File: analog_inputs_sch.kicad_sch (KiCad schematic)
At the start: 52 parts, among them J1 Conn_Coaxial, J2 Conn_Coaxial, K1 Relay_SPDT, K2 Relay_SPDT, K3 Relay_SPDT, K4 Relay_SPDT, K5 Relay_SPDT, K6 Relay_SPDT, U1 OPA656U, U15 OPA2277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

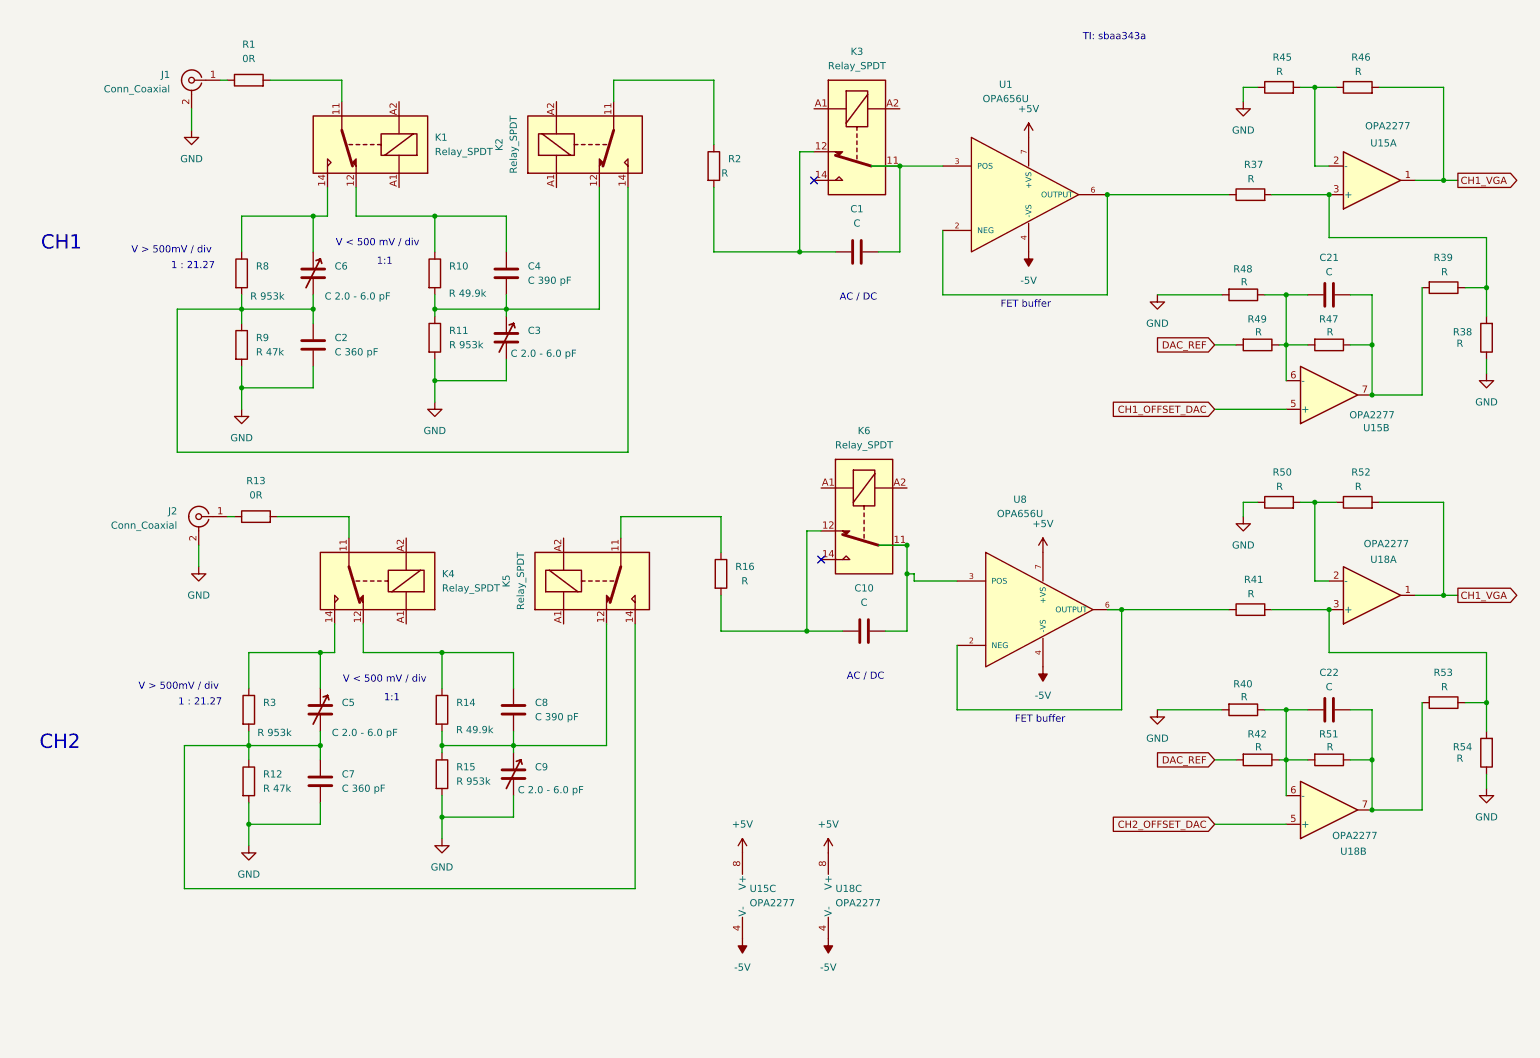
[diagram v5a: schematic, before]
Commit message: PCB edge, initial work on assigning footprints
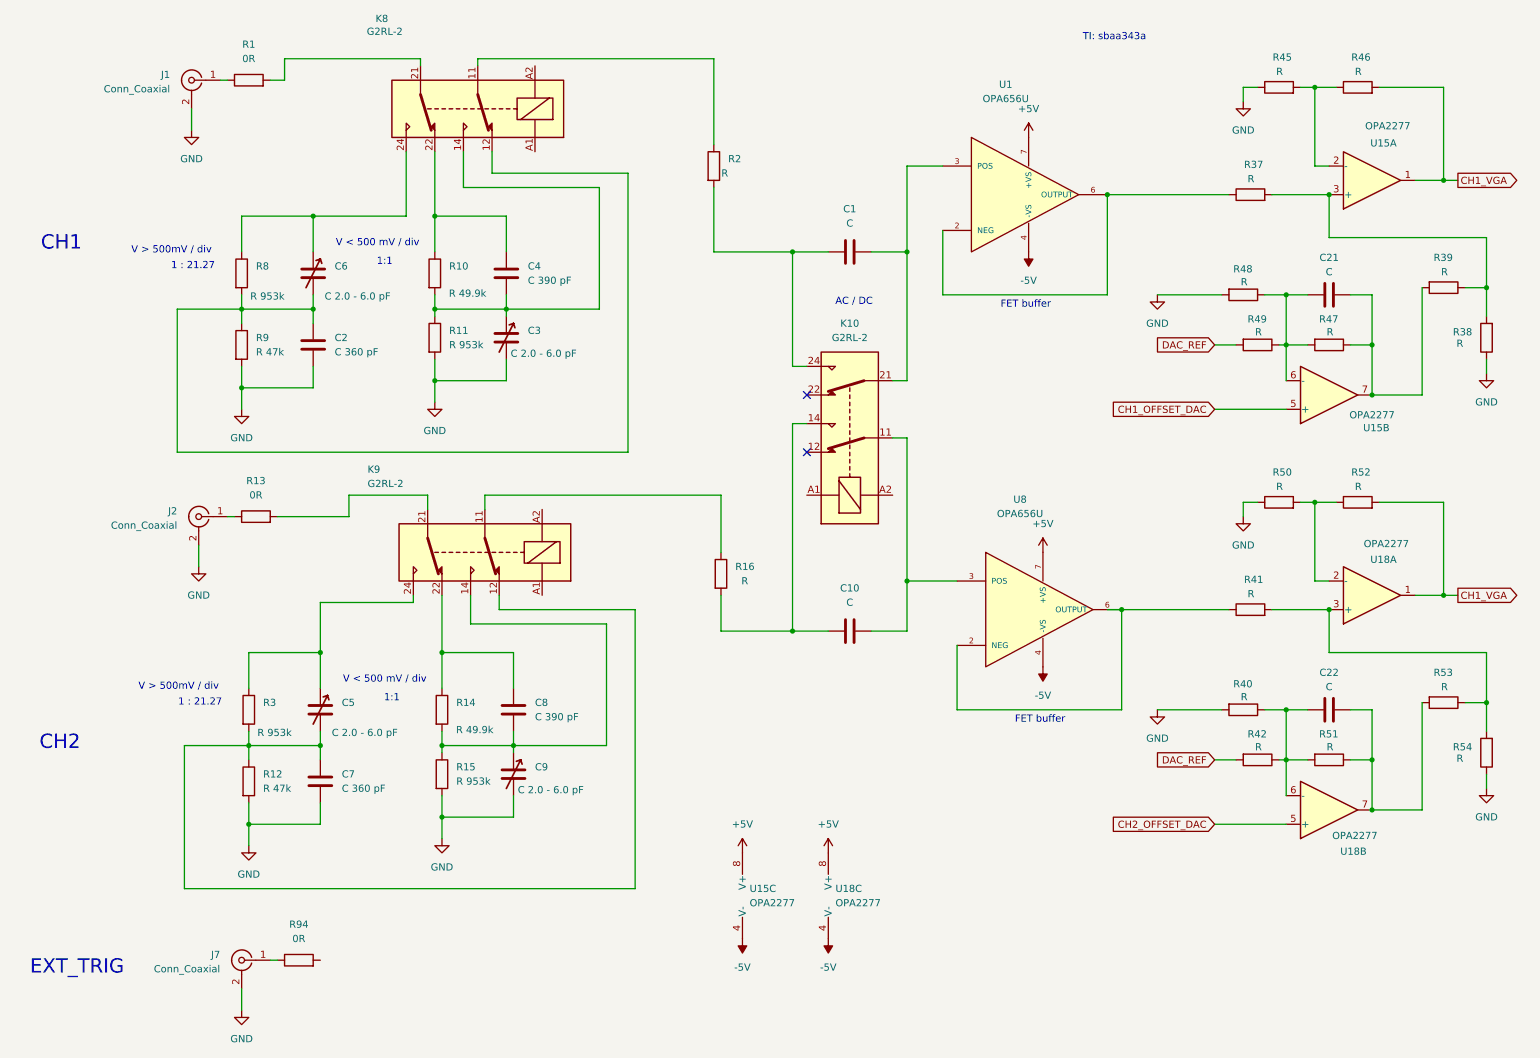
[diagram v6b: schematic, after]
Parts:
- removed K1, K2, K3, K4, K5, K6: Relay_SPDT, symbol Relay:Relay_SPDT
- added J7: Conn_Coaxial, Connector_Coaxial:BNC_TEConnectivity_1478035_Horizontal, symbol Connector:Conn_Coaxial
- added K10, K8, K9: G2RL-2, Relay_THT:Relay_DPDT_Omron_G2RL-2, symbol Relay:G2RL-2
- added R94: 0R, symbol Device:R
- J1, J2: footprint (none) -> Connector_Coaxial:BNC_TEConnectivity_1478035_Horizontal
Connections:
- net GND: now also J7.2 (Ext)
- net at C5.2, C7.1, R12.1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: now also K9.12
- net at R16.1: now also K9.11
- net at C10.1, R16.2: now also K10.14
- net at C4.1, R10.1: now also K8.22
- net at C3.1, C4.2, R10.2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: now also K8.14
- net at C10.2, U8.3 (POS): now also K10.11
- net at C8.1, R14.1: now also K9.22
- net at C8.2, C9.1, R14.2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: now also K9.14
- net at R13.2: now also K9.21
- net at C5.1, R3.1: now also K9.24
- net at C2.1, C6.2, R8.2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: now also K8.12
- net at C1.1, R2.2: now also K10.24
- net at C1.2, U1.3 (POS): now also K10.21
- net at R1.2: now also K8.21
- net at C6.1, R8.1: now also K8.24
- net at R2.1: now also K8.11
- new net: J7.1 (In), R94.1
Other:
- note added: "EXT_TRIG"
- moved on the sheet: C1, C10
